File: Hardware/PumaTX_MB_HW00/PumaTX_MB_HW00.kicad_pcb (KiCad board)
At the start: 2 copper layers, 32 parts, among them J100 FH12A-26S-0.5SH_55_, J102 500334-0160, J103 500334-0160, J104 692122030100, J105 Conn_01x02_Male, J106 Conn_01x02_Male, J107 Conn_01x02_Male, J410 U.FL-R-SMT-1_40_, Q200 UMH3NTN, Q201 UMH3NTN, U200 CP2105-F01-GMR, U300 ESP32-PICO-D4, U400 ESP32-PICO-D4, U402 E28-2G4M27S, U410 SX1280

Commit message: quick schematic update
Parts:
- added J105: 53398-0667, Component_lib:533980667, F.Cu at (248.8, 105.8)
- added U500: BQ24075RGTR, Component_lib:QFN50P300X300X100-17N-D, F.Cu at (243.2, 113.0)
- added U510: MIC5528-3.3YMT-T5, Component_lib:SON40P120X120X60-7N-D, F.Cu at (223.2, 125.9)
- added U520: MIC5528-3.3YMT-T5, Component_lib:SON40P120X120X60-7N-D, F.Cu at (226.7, 125.9)
- added U530: MIC5528-3.3YMT-T5, Component_lib:SON40P120X120X60-7N-D, F.Cu at (258.8, 103.9)
- moved J104 7.05 mm to (142.0, 154.8)
- renumbered J105 to J106, J106 to J107, J107 to J108
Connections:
- J104 pad 1: unconnected-(J104-Pad1) -> VBUS
- J104 pad 2: unconnected-(J104-Pad2) -> Net-(J104-Pad2)
- J104 pad 3: unconnected-(J104-Pad3) -> /PUMATX_ESP32_3V3
- J104 pad 4: unconnected-(J104-Pad4) -> GND
- J104 pad 6: unconnected-(J104-Pad6) -> /CRSF
- J104 pad 8: unconnected-(J104-Pad8) -> /PUMATX_SDA
- J104 pad 9: unconnected-(J104-Pad9) -> /PUMATX_SCL
- J104 pad MH1: unconnected-(J104-PadMH1) -> GND
- J104 pad MH2: unconnected-(J104-PadMH2) -> GND
- U200 pad 3: unconnected-(U200-Pad3) -> /D+
- U200 pad 4: unconnected-(U200-Pad4) -> /D-
- U402 pad 1: unconnected-(U402-Pad1) -> /SX1280_3V3

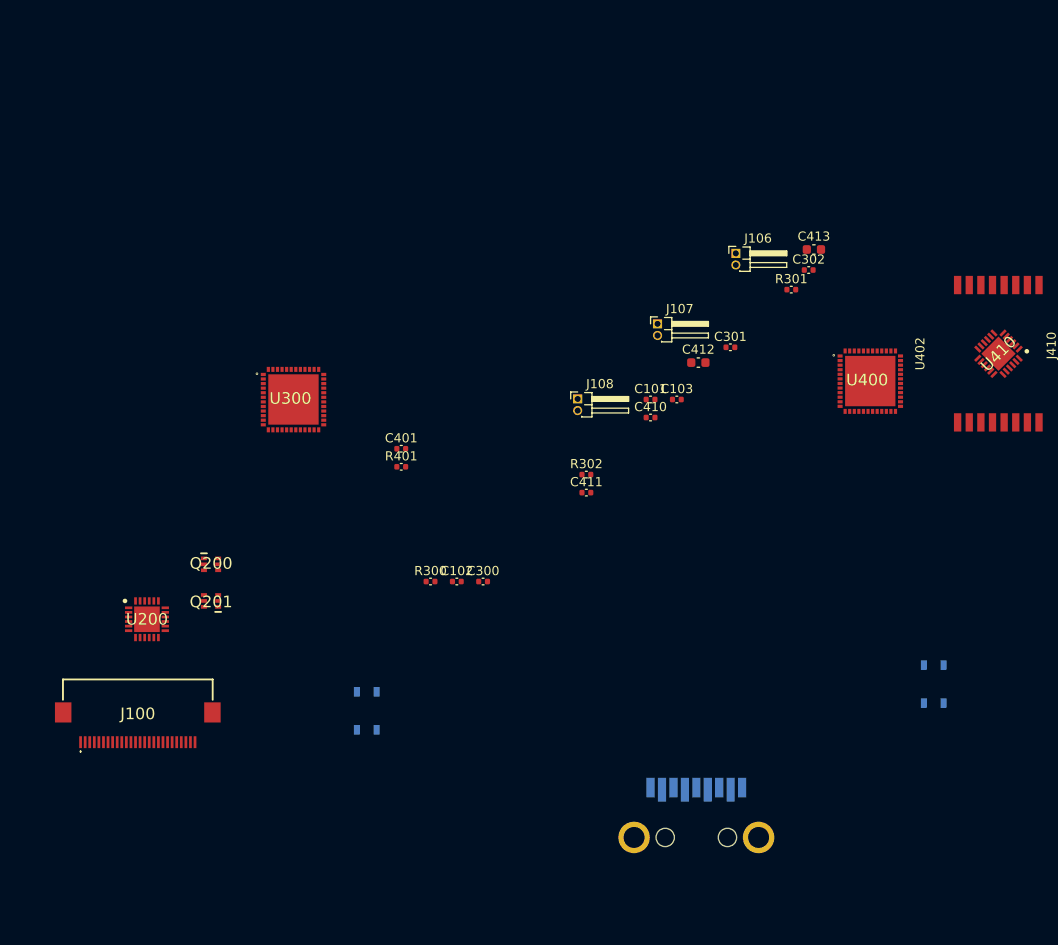
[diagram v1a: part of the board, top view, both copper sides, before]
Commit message: Added some footprints
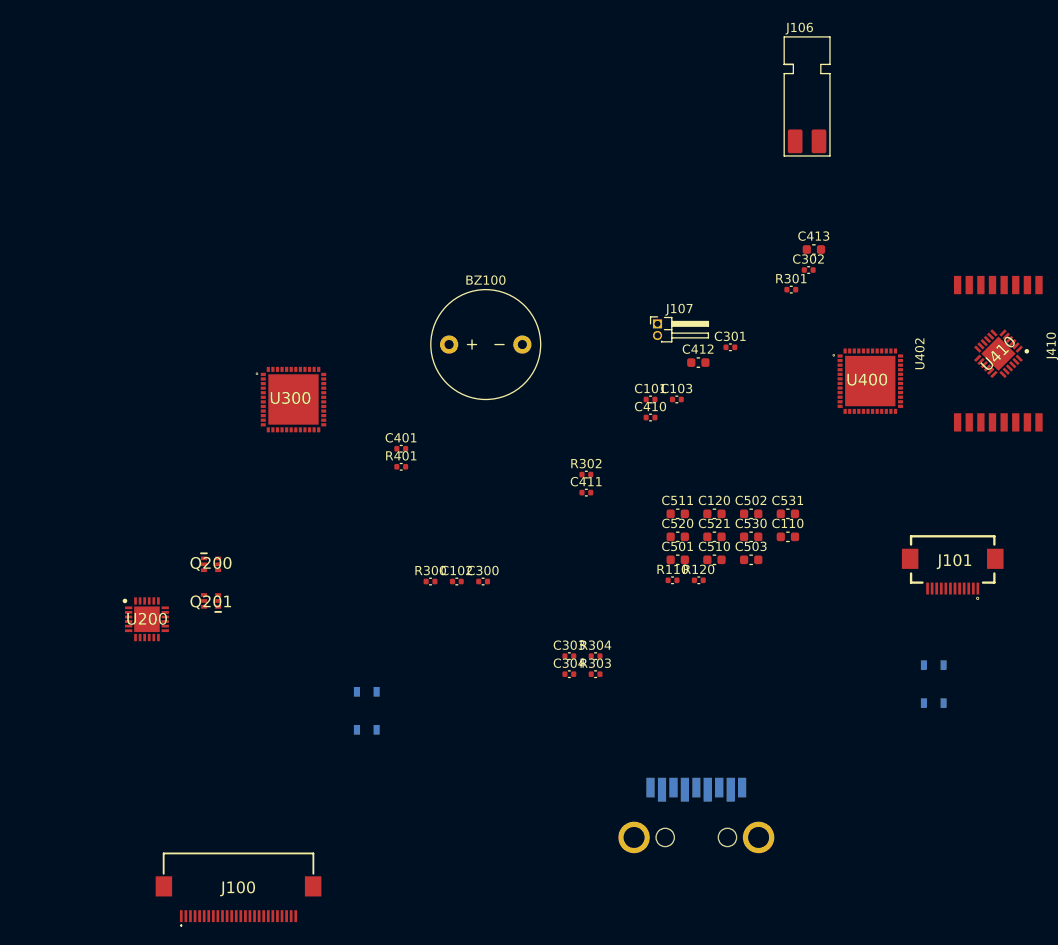
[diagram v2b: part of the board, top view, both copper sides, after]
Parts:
- removed J108: Conn_01x02_Male, Connector_PinHeader_1.27mm:PinHeader_1x02_P1.27mm_Horizontal
- added BZ100: Buzzer, Component_lib:GL200A_BUZZER, F.Cu at (119.0, 101.0)
- added C110: 100n, Capacitor_SMD:C_0603_1608Metric, F.Cu at (152.0, 122.0)
- added C120: 100n, Capacitor_SMD:C_0603_1608Metric, F.Cu at (144.0, 119.5)
- added C303: 15u, Capacitor_SMD:C_0402_1005Metric, F.Cu at (128.1, 135.0)
- added C304: 15u, Capacitor_SMD:C_0402_1005Metric, F.Cu at (128.1, 137.0)
- added C501: 1u, Capacitor_SMD:C_0603_1608Metric, F.Cu at (140.0, 124.5)
- added C502: 4u7, Capacitor_SMD:C_0603_1608Metric, F.Cu at (148.0, 119.5)
- added C503: 4u7, Capacitor_SMD:C_0603_1608Metric, F.Cu at (148.0, 124.5)
- added C510: 2u2, Capacitor_SMD:C_0603_1608Metric, F.Cu at (144.0, 124.5)
- added C511: 2u2, Capacitor_SMD:C_0603_1608Metric, F.Cu at (140.0, 119.5)
- added C520: 2u2, Capacitor_SMD:C_0603_1608Metric, F.Cu at (140.0, 122.0)
- added C521: 2u2, Capacitor_SMD:C_0603_1608Metric, F.Cu at (144.0, 122.0)
- added C530: 2u2, Capacitor_SMD:C_0603_1608Metric, F.Cu at (148.0, 122.0)
- added C531: 2u2, Capacitor_SMD:C_0603_1608Metric, F.Cu at (152.0, 119.5)
- added J101: FH12-12S-0.5SH_55_, Component_lib:FH12-12S-0.5SH_55_, F.Cu at (170.0, 127.0)
- added R110: 4k7, Capacitor_SMD:C_0402_1005Metric, F.Cu at (139.4, 126.8)
- added R120: 4k7, Capacitor_SMD:C_0402_1005Metric, F.Cu at (142.3, 126.8)
- added R303: 2k2, Capacitor_SMD:C_0402_1005Metric, F.Cu at (131.0, 137.0)
- added R304: 2k2, Capacitor_SMD:C_0402_1005Metric, F.Cu at (131.0, 135.0)
- J106: footprint Connector_PinHeader_1.27mm:PinHeader_1x02_P1.27mm_Horizontal -> Component_lib:GL200A_HAPTIC_MOTOR
- moved J100 22.0 mm to (92.0, 160.0)
- moved J106 11.9 mm to (151.6, 80.4)
- renumbered S100 to S110, S101 to S120
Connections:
- J100 pad 1: unconnected-(J100-Pad1) -> /PHOTO
- J100 pad 10: unconnected-(J100-Pad10) -> /LED_ANODE
- J100 pad 11: unconnected-(J100-Pad11) -> /PAUSE
- J100 pad 12: unconnected-(J100-Pad12) -> GND
- J100 pad 13: unconnected-(J100-Pad13) -> /ON_OFF
- J100 pad 14: unconnected-(J100-Pad14) -> /LED_CATHODE
- J100 pad 16: unconnected-(J100-Pad16) -> GND
- J100 pad 18: unconnected-(J100-Pad18) -> GND
- J100 pad 19: unconnected-(J100-Pad19) -> GND
- J100 pad 2: unconnected-(J100-Pad2) -> /RECORD
- J100 pad 20: unconnected-(J100-Pad20) -> /D+
- J100 pad 21: unconnected-(J100-Pad21) -> /D-
- J100 pad 22: unconnected-(J100-Pad22) -> VBUS
- J100 pad 23: unconnected-(J100-Pad23) -> VBUS
- J100 pad 24: unconnected-(J100-Pad24) -> VBUS
- J100 pad 25: unconnected-(J100-Pad25) -> VBUS
- J100 pad 26: unconnected-(J100-Pad26) -> VBUS
- J100 pad 3: unconnected-(J100-Pad3) -> /DOWN
- J100 pad 4: unconnected-(J100-Pad4) -> /RIGHT
- J100 pad 5: unconnected-(J100-Pad5) -> GND
- J100 pad 6: unconnected-(J100-Pad6) -> /LEFT
- J100 pad 7: unconnected-(J100-Pad7) -> /OK
- J100 pad 8: unconnected-(J100-Pad8) -> /UP
- J100 pad 9: unconnected-(J100-Pad9) -> /RTH
- J104 pad 8: /PUMATX_SDA -> /DISPLAY_SDA
- J104 pad 9: /PUMATX_SCL -> /DISPLAY_SCL
- S110 pad 3: unconnected-(S100-Pad3) -> GND
- S110 pad 4: unconnected-(S100-Pad4) -> GND
- S120 pad 3: unconnected-(S101-Pad3) -> GND
- S120 pad 4: unconnected-(S101-Pad4) -> GND
- U300 pad 16: /BUZZER_PWM -> /DISPLAY_SCL
- U300 pad 17: /FAN_PWM -> /DISPLAY_SDA
- U400 pad 13: unconnected-(U400-Pad13) -> /FAN_PWM
- U400 pad 14: unconnected-(U400-Pad14) -> /BUZZER_PWM

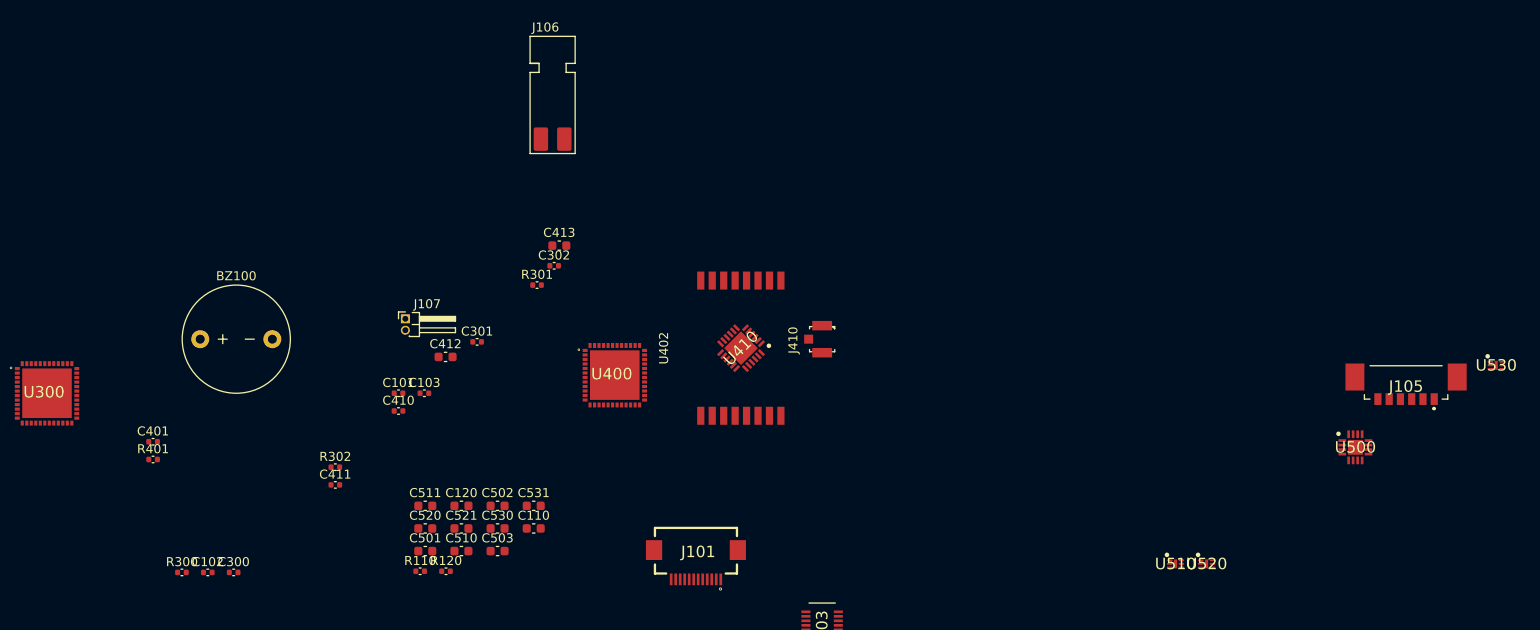
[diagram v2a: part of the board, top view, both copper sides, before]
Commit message: Schematic is "done"
Functionaly it is done, but could get some cleanup
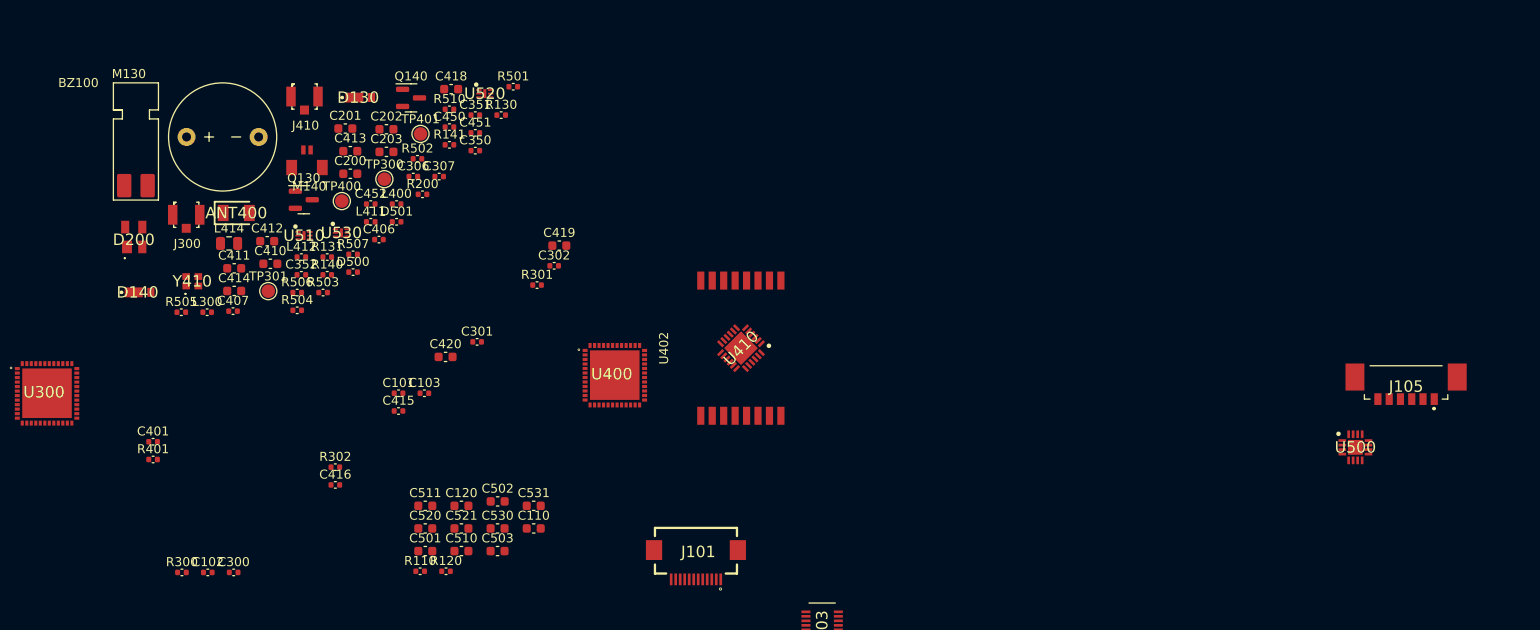
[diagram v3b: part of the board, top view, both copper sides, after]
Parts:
- removed J106: Conn_01x02_Male, Component_lib:GL200A_HAPTIC_MOTOR
- removed J107: Conn_01x02_Male, Connector_PinHeader_1.27mm:PinHeader_1x02_P1.27mm_Horizontal
- added ANT400: 2450AT18A100E, Component_lib:ANTC3216X140N, F.Cu at (119.0, 87.0)
- added C200: 1u, Capacitor_SMD:C_0603_1608Metric, F.Cu at (131.7, 82.7)
- added C201: 100n, Capacitor_SMD:C_0603_1608Metric, F.Cu at (131.1, 77.6)
- added C202: 1u, Capacitor_SMD:C_0603_1608Metric, F.Cu at (135.7, 77.7)
- added C203: 100n, Capacitor_SMD:C_0603_1608Metric, F.Cu at (135.7, 80.2)
- added C306: C, Capacitor_SMD:C_0402_1005Metric, F.Cu at (138.6, 83.0)
- added C307: C, Capacitor_SMD:C_0402_1005Metric, F.Cu at (141.5, 83.0)
- added C350: 100n, Capacitor_SMD:C_0402_1005Metric, F.Cu at (145.5, 80.1)
- added C351: 1u, Capacitor_SMD:C_0402_1005Metric, F.Cu at (145.5, 76.1)
- added C352: 10u, Capacitor_SMD:C_0402_1005Metric, F.Cu at (126.2, 93.9)
- added C406: C, Capacitor_SMD:C_0402_1005Metric, F.Cu at (134.8, 90.0)
- added C407: C, Capacitor_SMD:C_0402_1005Metric, F.Cu at (118.6, 97.9)
- added C410: 0p8, Capacitor_SMD:C_0603_1608Metric, F.Cu at (122.8, 92.6)
- added C411: 1p2, Capacitor_SMD:C_0603_1608Metric, F.Cu at (118.8, 93.1)
- added C412: 1p2, Capacitor_SMD:C_0603_1608Metric, F.Cu at (122.4, 90.1)
- added C413: 100p, Capacitor_SMD:C_0603_1608Metric, F.Cu at (131.7, 80.1)
- added C414: 0p5, Capacitor_SMD:C_0603_1608Metric, F.Cu at (118.8, 95.7)
- added C418: 100n, Capacitor_SMD:C_0603_1608Metric, F.Cu at (142.8, 73.3)
- added C450: 100n, Capacitor_SMD:C_0402_1005Metric, F.Cu at (142.7, 77.5)
- added C451: 1u, Capacitor_SMD:C_0402_1005Metric, F.Cu at (145.5, 78.1)
- added C452: 10u, Capacitor_SMD:C_0402_1005Metric, F.Cu at (133.9, 86.0)
- added D130: S1GHE, Component_lib:S1GHE, F.Cu at (132.9, 74.2)
- added D140: S1GHE, Component_lib:S1GHE, F.Cu at (108.4, 95.8)
- added D200: SP0503BAHTG, Component_lib:SP0503BAHTG, F.Cu at (107.6, 89.7)
- added D500: LED, Capacitor_SMD:C_0402_1005Metric, F.Cu at (132.0, 93.6)
- added D501: LED, Capacitor_SMD:C_0402_1005Metric, F.Cu at (136.8, 88.0)
- added J300: U.FL-R-SMT-1_40_, Component_lib:u.fl, F.Cu at (113.5, 87.2)
- added L300: L, Capacitor_SMD:C_0402_1005Metric, F.Cu at (115.8, 98.0)
- added L400: L, Capacitor_SMD:C_0402_1005Metric, F.Cu at (136.8, 86.0)
- added L411: 3n, Capacitor_SMD:C_0402_1005Metric, F.Cu at (133.9, 88.0)
- added L412: 2n5, Capacitor_SMD:C_0402_1005Metric, F.Cu at (126.2, 91.9)
- added L414: 15u, Capacitor_SMD:C_0805_2012Metric, F.Cu at (118.2, 90.4)
- added M130: Motor_DC, Component_lib:GL200A_HAPTIC_MOTOR, F.Cu at (105.4, 85.6)
- added M140: Fan, Component_lib:SM02B-SURS-TF, F.Cu at (126.8, 80.5)
- added Q130: ZXMN3B01F, Package_TO_SOT_SMD:SOT-23, F.Cu at (126.5, 85.5)
- added Q140: ZXMN3B01F, Package_TO_SOT_SMD:SOT-23, F.Cu at (138.4, 74.2)
- added R130: 10k, Capacitor_SMD:C_0402_1005Metric, F.Cu at (148.4, 76.1)
- added R131: 180, Capacitor_SMD:C_0402_1005Metric, F.Cu at (129.1, 91.9)
- added R140: 10k, Capacitor_SMD:C_0402_1005Metric, F.Cu at (129.1, 93.9)
- added R141: 180, Capacitor_SMD:C_0402_1005Metric, F.Cu at (142.7, 79.4)
- added R200: 4k7, Capacitor_SMD:C_0402_1005Metric, F.Cu at (139.7, 84.9)
- added R501: 100k, Capacitor_SMD:C_0402_1005Metric, F.Cu at (149.7, 73.0)
- added R502: 1k1, Capacitor_SMD:C_0402_1005Metric, F.Cu at (139.1, 81.0)
- added R503: 590, Capacitor_SMD:C_0402_1005Metric, F.Cu at (128.6, 95.8)
- added R504: 0, Capacitor_SMD:C_0402_1005Metric, F.Cu at (125.8, 97.8)
- added R505: 36k5, Capacitor_SMD:C_0402_1005Metric, F.Cu at (112.9, 98.0)
- added R506: 1k5, Capacitor_SMD:C_0402_1005Metric, F.Cu at (125.8, 95.8)
- added R507: 1k5, Capacitor_SMD:C_0402_1005Metric, F.Cu at (132.0, 91.6)
- added R510: 0k, Capacitor_SMD:C_0402_1005Metric, F.Cu at (142.7, 75.5)
- added TP300: PUMATX_PU, TestPoint:TestPoint_Pad_D1.5mm, F.Cu at (135.4, 83.2)
- added TP301: VDD_SDIO, TestPoint:TestPoint_Pad_D1.5mm, F.Cu at (122.5, 95.7)
- added TP400: TestPoint, TestPoint:TestPoint_Pad_D1.5mm, F.Cu at (130.7, 85.7)
- added TP401: VDD_SDIO, TestPoint:TestPoint_Pad_D1.5mm, F.Cu at (139.4, 78.2)
- added Y410: NX2016SA-52MHZ-EXS00A-CS06016, Component_lib:NX2016SA32MEXS00ACS06465, F.Cu at (114.1, 94.6)
- moved U530 129.0 mm to (130.7, 89.2)
- moved U510 103.3 mm to (126.5, 89.5)
- moved U520 95.6 mm to (146.6, 73.8)
- moved J410 63.4 mm to (126.6, 74.1), turned to 0 degrees
- moved BZ100 22.5 mm to (117.5, 78.6)
- moved C502 0.49 mm to (148.0, 119.0)
- renumbered C410 to C415, C411 to C416, C413 to C419, C412 to C420
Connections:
- net /IRS renamed /V_DCC
- net Net-(C101-Pad1) renamed /DISPLAY_DECOUPLE_1
- net Net-(C102-Pad1) renamed /DISPLAY_DECOUPLE_2
- net Net-(C410-Pad1) renamed /V_PA
- BZ100 pad 1: unconnected-(BZ100-Pad1) -> /BUZZER_PWM
- BZ100 pad 2: unconnected-(BZ100-Pad2) -> GND
- C110 pad 1: /PUMATX_ESP32_3V3 -> +3V3
- C120 pad 1: /PUMATX_ESP32_3V3 -> +3V3
- C420 pad 1: /3V3_ELRS -> /SX1280_3V3
- C503 pad 1: Net-(C503-Pad1) -> /VBAT
- C510 pad 1: Net-(C510-Pad1) -> /VSYS
- C511 pad 1: /PUMATX_ESP32_3V3 -> +3V3
- C521 pad 1: /ELRS_ESP32_3V3 -> -3V3
- J100 pad MP1: unconnected-(J100-PadMP1) -> GND
- J100 pad MP2: unconnected-(J100-PadMP2) -> GND
- J104 pad 2: Net-(J104-Pad2) -> /VSYS
- J104 pad 3: /PUMATX_ESP32_3V3 -> +3V3
- J104 pad 5: unconnected-(J104-Pad5) -> /TX_PUMATX_DEBUG
- J104 pad 6: /CRSF -> /RX_PUMATX_DEBUG
- J104 pad 7: unconnected-(J104-Pad7) -> /CRSF
- J105 pad 5: Net-(J105-Pad5) -> /VBAT
- J105 pad 6: Net-(J105-Pad5) -> /VBAT
- J105 pad MP1: unconnected-(J105-PadMP1) -> GND
- J105 pad MP2: unconnected-(J105-PadMP2) -> GND
- J410 pad 1: Net-(J410-Pad1) -> /50_ELRS_ANT_4
- R110 pad 1: /PUMATX_ESP32_3V3 -> +3V3
- R120 pad 1: /PUMATX_ESP32_3V3 -> +3V3
- R401 pad 1: +3V3 -> -3V3
- U200 pad 2: unconnected-(U200-Pad2) -> GND
- U200 pad 25: unconnected-(U200-Pad25) -> GND
- U200 pad 5: unconnected-(U200-Pad5) -> +3V3
- U200 pad 6: unconnected-(U200-Pad6) -> /3V45
- U200 pad 7: unconnected-(U200-Pad7) -> VBUS
- U200 pad 8: unconnected-(U200-Pad8) -> VBUS
- U200 pad 9: unconnected-(U200-Pad9) -> /RST
- U300 pad 1: unconnected-(U300-Pad1) -> +3V3
- U300 pad 19: unconnected-(U300-Pad19) -> +3V3
- U300 pad 2: unconnected-(U300-Pad2) -> /50_PUMATX_ANT_1
- U300 pad 26: unconnected-(U300-Pad26) -> /VDD_SDIO_PUMATX
- U300 pad 3: unconnected-(U300-Pad3) -> +3V3
- U300 pad 37: unconnected-(U300-Pad37) -> +3V3
- U300 pad 4: unconnected-(U300-Pad4) -> +3V3
- U300 pad 43: unconnected-(U300-Pad43) -> +3V3
- U300 pad 46: unconnected-(U300-Pad46) -> +3V3
- U400 pad 1: unconnected-(U400-Pad1) -> -3V3
- U400 pad 19: unconnected-(U400-Pad19) -> -3V3
- U400 pad 2: unconnected-(U400-Pad2) -> /50_ESP_ELRS_ANT_1
- U400 pad 26: unconnected-(U400-Pad26) -> /VDD_SDIO_ELRS
- U400 pad 3: unconnected-(U400-Pad3) -> -3V3
- U400 pad 37: unconnected-(U400-Pad37) -> -3V3
- U400 pad 4: unconnected-(U400-Pad4) -> -3V3
- U400 pad 43: unconnected-(U400-Pad43) -> -3V3
- U400 pad 46: unconnected-(U400-Pad46) -> -3V3
- U410 pad 11: /3V3_ELRS -> /SX1280_3V3
- U410 pad 14: unconnected-(U410-Pad14) -> /V_DCC2
- U410 pad 15: /3V3_ELRS -> /SX1280_3V3
- U410 pad 22: Net-(J410-Pad1) -> /50_ELRS_ANT_1
- U410 pad 4: unconnected-(U410-Pad4) -> /XTA
- U410 pad 6: unconnected-(U410-Pad6) -> /XTB
- U500 pad 10: Net-(U500-Pad10) -> /VSYS
- U500 pad 11: Net-(U500-Pad10) -> /VSYS
- U500 pad 12: unconnected-(U500-Pad12) -> /ILIM
- U500 pad 14: unconnected-(U500-Pad14) -> /TMR
- U500 pad 15: unconnected-(U500-Pad15) -> /SYSOFF
- U500 pad 16: unconnected-(U500-Pad16) -> /ISET
- U500 pad 2: Net-(U500-Pad2) -> /VBAT
- U500 pad 3: Net-(U500-Pad2) -> /VBAT
- U500 pad 4: unconnected-(U500-Pad4) -> /BQ_CE
- U500 pad 5: unconnected-(U500-Pad5) -> /VSYS
- U500 pad 6: unconnected-(U500-Pad6) -> GND
- U500 pad 7: unconnected-(U500-Pad7) -> /BQ_PGOOD
- U500 pad 9: unconnected-(U500-Pad9) -> /BQ_CHG
- U510 pad 1: /PUMATX_ESP32_3V3 -> +3V3
- U510 pad 2: /PUMATX_ESP32_3V3 -> +3V3
- U510 pad 4: unconnected-(U510-Pad4) -> /3V3_EN
- U510 pad 6: Net-(C510-Pad1) -> /VSYS
- U520 pad 1: /ELRS_ESP32_3V3 -> -3V3
- U520 pad 2: /ELRS_ESP32_3V3 -> -3V3
- U520 pad 4: unconnected-(U520-Pad4) -> /LED
- U530 pad 4: unconnected-(U530-Pad4) -> /LED
